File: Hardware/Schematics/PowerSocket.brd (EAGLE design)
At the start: 100 x 47.5 mm, 74 parts, among them T1 BT138-V, T2 BT138-V, T3 BT138-V, T4 BT138-V, T5 BT138-V, T6 BT138-V

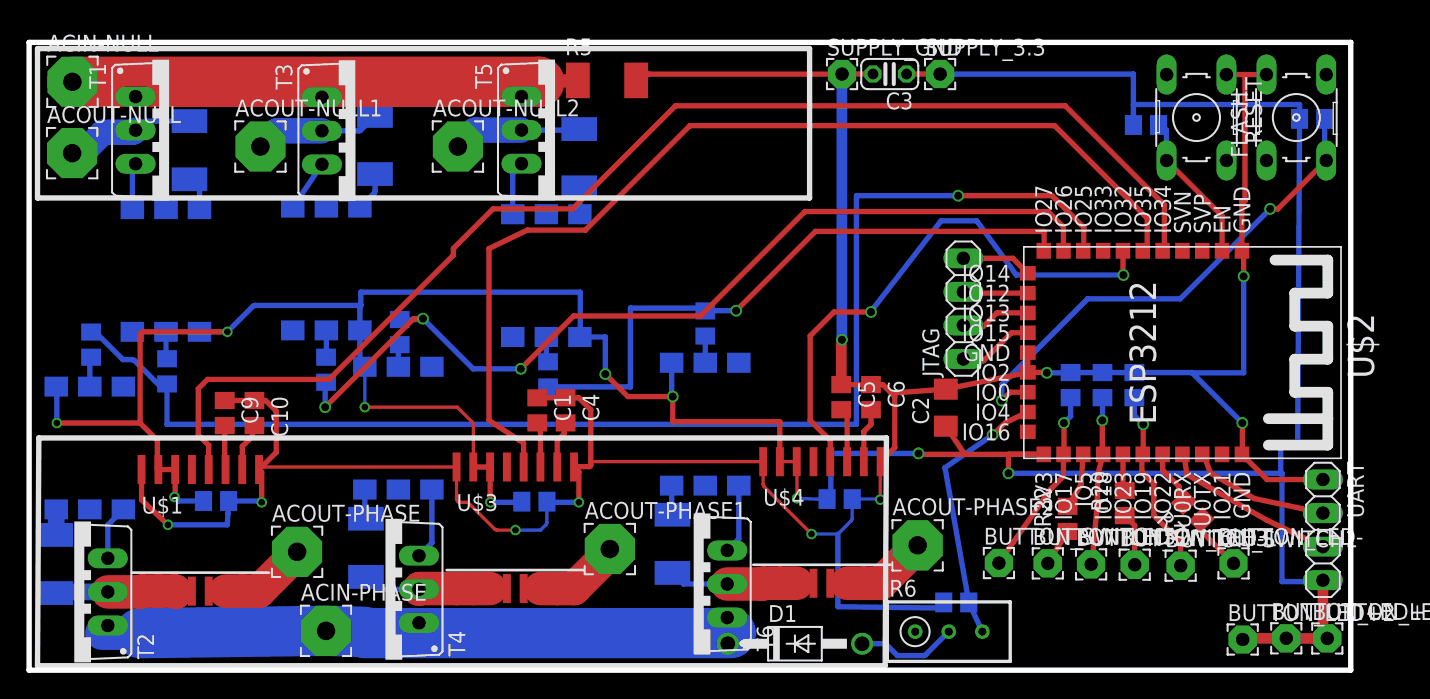
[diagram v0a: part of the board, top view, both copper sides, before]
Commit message: Added more clearance to GND planes.
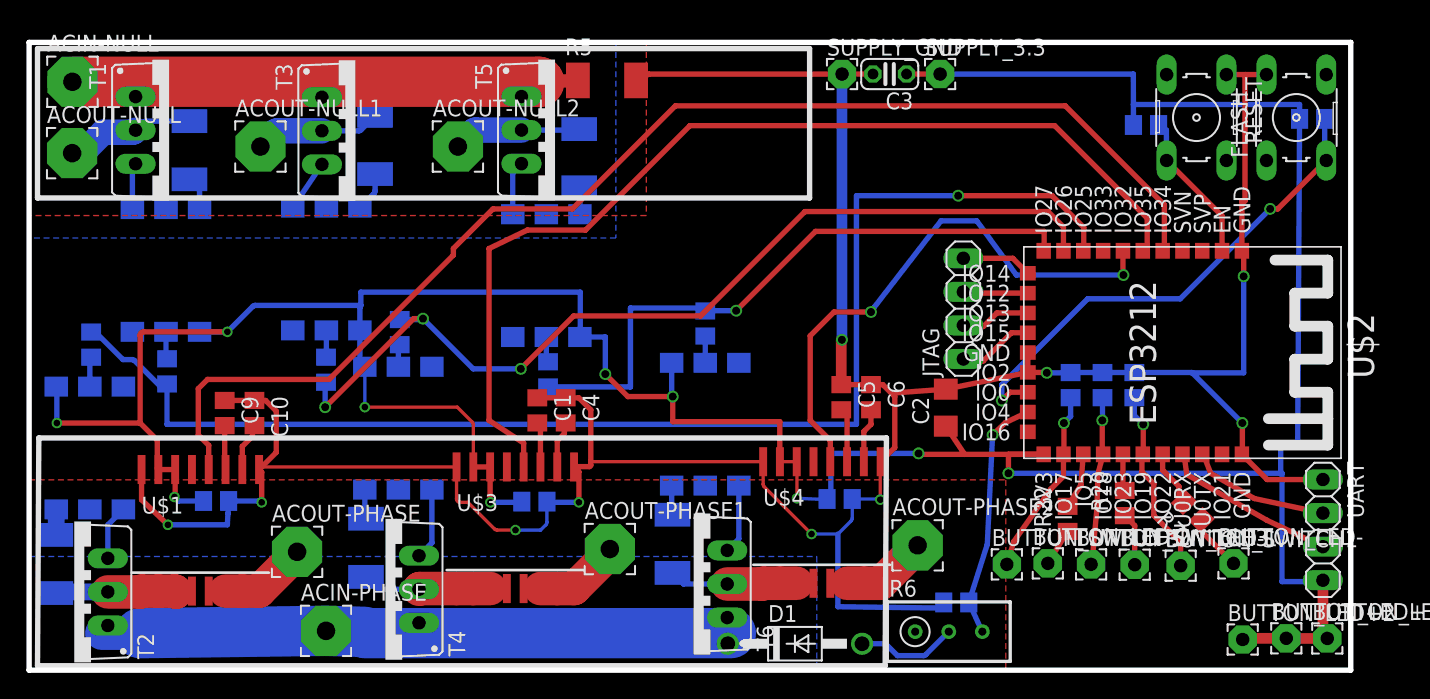
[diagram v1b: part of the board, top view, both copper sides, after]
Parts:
- moved BUTTON_SWITCH5 0.61 mm to (74.0, 9.11)
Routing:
- net N$3: track 20.4 -> 18.6 mm
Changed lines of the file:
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@@
 <element name="BUTTON_LED+2" library="wirepad" package="2,15/1,0" value="-" x="91.825" y="3.42"/>
 <element name="R22" library="rcl" package="R0805" value="100" x="78.58" y="12.545" rot="R90"/>
-<element name="BUTTON_SWITCH5" library="wirepad" package="2,15/1,0" value="-" x="73.38" y="9.205"/>
+<element name="BUTTON_SWITCH5" library="wirepad" package="2,15/1,0" value="-" x="73.98" y="9.105"/>
 <element name="R23" library="rcl" package="R0805" value="10K" x="78.805" y="22.67" rot="MR270"/>
 <element name="JTAG" library="pinhead" package="1X04" value="-" x="70.69" y="28.455" rot="R90"/>
@@
 <wire x1="61.5" y1="26.1" x2="61.5" y2="46.195" width="0.8128" layer="16"/>
 <wire x1="61.5" y1="46.195" x2="61.51" y2="46.205" width="0.8128" layer="16"/>
-<polygon width="0.4064" layer="16" isolate="0.8128">
-<vertex x="0" y="1.2"/>
-<vertex x="0" y="48.6"/>
+<polygon width="0.4064" layer="16" isolate="0.254">
+<vertex x="0" y="9.7"/>
+<vertex x="59.6" y="9.7"/>
+<vertex x="59.6" y="1.1"/>
+<vertex x="100" y="1.1"/>
 <vertex x="100" y="48.6"/>
-<vertex x="100" y="48.5"/>
-<vertex x="100" y="1"/>
-<vertex x="0" y="1"/>
+<vertex x="44.4" y="48.6"/>
+<vertex x="44.4" y="33.8"/>
+<vertex x="0" y="33.8"/>
 </polygon>
 </signal>
@@
 <wire x1="72.125" y1="4.015" x2="72.105" y2="4.035" width="0.4064" layer="16"/>
 <wire x1="72.105" y1="4.035" x2="71.105" y2="6.225" width="0.4064" layer="16"/>
-<wire x1="71.105" y1="6.225" x2="69.3" y2="16.42" width="0.4064" layer="16"/>
-<wire x1="69.3" y1="16.42" x2="72.9" y2="18.9" width="0.4064" layer="16"/>
+<wire x1="71.105" y1="6.225" x2="72.5" y2="10.62" width="0.4064" layer="16"/>
+<wire x1="72.5" y1="10.62" x2="72.9" y2="18.9" width="0.4064" layer="16"/>
 <via x="72.9" y="18.9" extent="1-16" drill="0.6" shape="square"/>
 <wire x1="72.9" y1="18.9" x2="73.87" y2="19.83" width="0.4064" layer="1"/>
@@
 <wire x1="78.3" y1="19.8" x2="78.3" y2="17.465" width="0.4064" layer="1"/>
 <wire x1="78.3" y1="17.465" x2="78.265" y2="17.43" width="0.4064" layer="1"/>
-<wire x1="73.38" y1="9.205" x2="74.5" y2="10.825" width="0.4064" layer="1"/>
+<wire x1="73.98" y1="9.105" x2="74.5" y2="10.825" width="0.4064" layer="1"/>
 <wire x1="74.5" y1="10.825" x2="77.3" y2="14.8" width="0.4064" layer="1"/>
 <wire x1="77.3" y1="14.8" x2="78.265" y2="15.765" width="0.4064" layer="1"/>
@@
 </signal>
 <signal name="N$37">
-<polygon width="0.4064" layer="1" isolate="0.8128">
+<polygon width="0.4064" layer="1">
+<vertex x="0" y="15.5"/>
+<vertex x="73.9" y="15.5"/>
+<vertex x="73.9" y="1.1"/>
 <vertex x="100" y="1.1"/>
-<vertex x="0" y="1.1"/>
-<vertex x="0" y="48.6"/>
 <vertex x="100" y="48.6"/>
+<vertex x="46.7" y="48.6"/>
+<vertex x="46.7" y="35.5"/>
+<vertex x="0" y="35.5"/>
 </polygon>
 </signal>

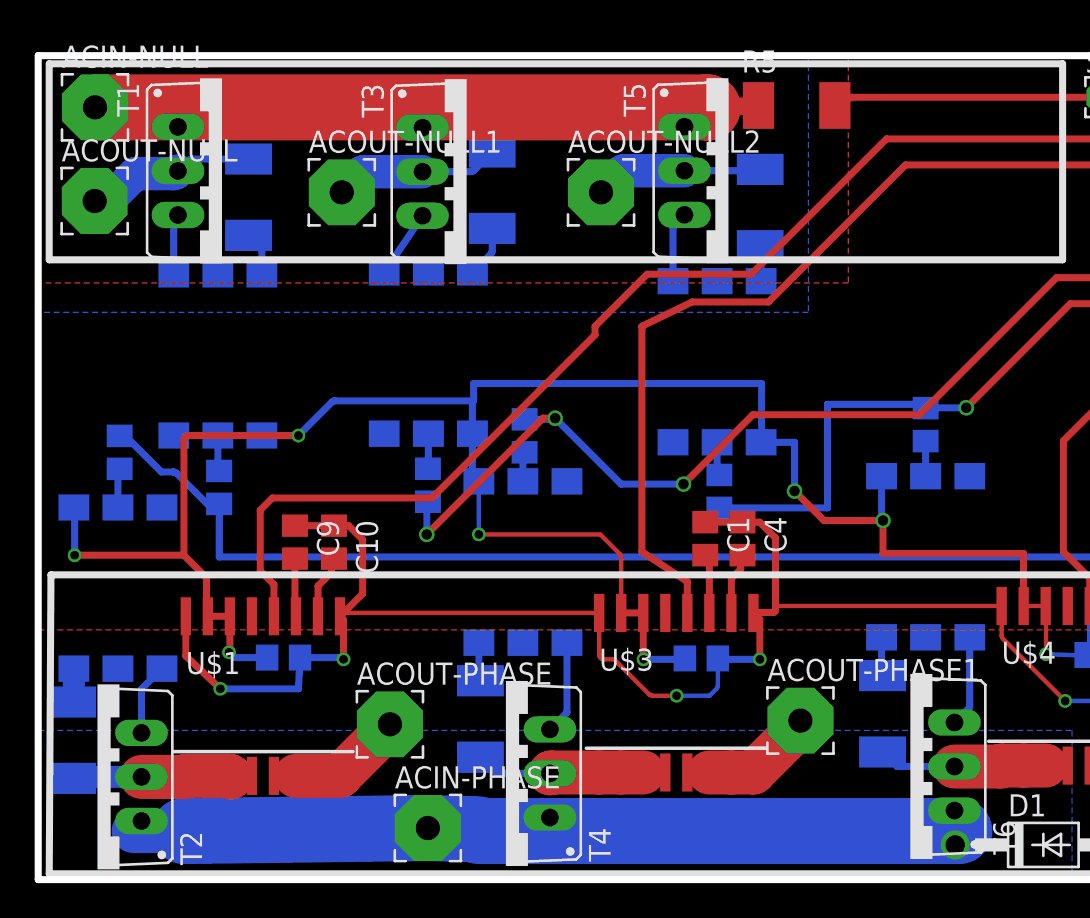
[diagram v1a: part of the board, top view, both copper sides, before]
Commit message: Run AC traces on both sides.
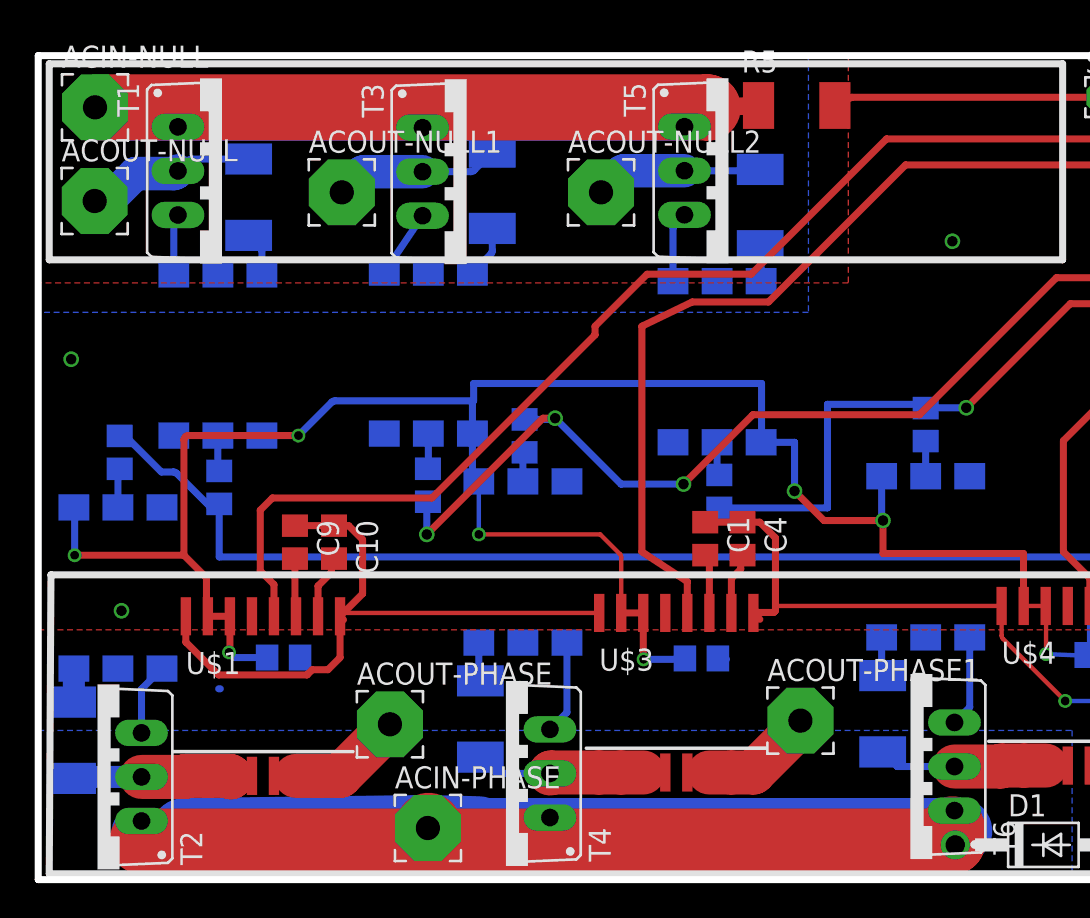
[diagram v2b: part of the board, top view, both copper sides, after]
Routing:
- net N$68: track 0.00 -> 48.6 mm
- net N$37: track 0.00 -> 34.3 mm
- net GND: track 232.6 -> 214.1 mm, vias 10 -> 6
- added copper zone on layer 1, net GND
- removed copper zone on layer 1, net N$37
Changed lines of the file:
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@@
 </class>
 </classes>
-<designrules name="dirt_cheap_dirty_boards.v1">
+<designrules name="dirt_cheap_dirty_boards.v1 *">
 <description language="en">&lt;b&gt;Dirty Cheap Dirty Board Design Rules&lt;/b&gt;
 &lt;br&gt;
@@
 <wire x1="18.7" y1="20.7" x2="18.7" y2="17.58" width="0.4064" layer="1"/>
 <wire x1="18.7" y1="17.58" x2="17.4" y2="16.28" width="0.4064" layer="1"/>
-<wire x1="15.095" y1="13.9" x2="15.045" y2="12.945" width="0.4064" layer="16"/>
-<wire x1="15.045" y1="12.945" x2="15" y2="12.1" width="0.4064" layer="16"/>
-<wire x1="15" y1="12.1" x2="10.5" y2="12.1" width="0.4064" layer="16"/>
 <wire x1="10.4" y1="12.1" x2="10.5" y2="12.1" width="0.4064" layer="16"/>
-<via x="10.5" y="12.1" extent="1-16" drill="0.5" shape="square"/>
-<wire x1="10.5" y1="12.1" x2="8.51" y2="13.99" width="0.4064" layer="1"/>
-<wire x1="8.51" y1="13.99" x2="8.51" y2="16.28" width="0.4064" layer="1"/>
 <wire x1="17.4" y1="16.28" x2="17.5" y2="16.18" width="0.4064" layer="1"/>
 <wire x1="17.4" y1="16.28" x2="17.6" y2="16.08" width="0.4064" layer="1"/>
-<wire x1="17.6" y1="16.08" x2="17.6" y2="13.8" width="0.4064" layer="1"/>
-<via x="17.6" y="13.8" extent="1-16" drill="0.5" shape="square"/>
-<wire x1="17.6" y1="13.8" x2="17.4" y2="13.9" width="0.4064" layer="16"/>
-<wire x1="17.4" y1="13.9" x2="15.095" y2="13.9" width="0.4064" layer="16"/>
 <wire x1="41.23" y1="16.475" x2="41.6" y2="16.105" width="0.4064" layer="1"/>
-<wire x1="41.6" y1="16.105" x2="41.6" y2="13.8" width="0.4064" layer="1"/>
-<via x="41.6" y="13.8" extent="1-16" drill="0.5" shape="square"/>
 <wire x1="39.18" y1="13.85" x2="39.68" y2="13.8" width="0.4064" layer="16"/>
-<wire x1="39.68" y1="13.8" x2="41.6" y2="13.8" width="0.4064" layer="16"/>
 <wire x1="64.43" y1="16.875" x2="64.4" y2="16.802575" width="0.254" layer="1" curve="45"/>
 <wire x1="64.4" y1="16.802575" x2="64.4" y2="14" width="0.254" layer="1"/>
@@
 <wire x1="64.4" y1="14" x2="64.279290625" y2="14.05" width="0.254" layer="16" curve="45"/>
 <wire x1="64.279290625" y1="14.05" x2="62.28" y2="14.05" width="0.254" layer="16"/>
-<wire x1="39.18" y1="13.85" x2="39.18" y2="12.285209375" width="0.254" layer="16"/>
-<wire x1="39.18" y1="12.285209375" x2="39.10560625" y2="12.10560625" width="0.254" layer="16" curve="-44.999502"/>
-<wire x1="39.10560625" y1="12.10560625" x2="38.7" y2="11.7" width="0.254" layer="16"/>
-<wire x1="38.7" y1="11.7" x2="36.8" y2="11.7" width="0.254" layer="16"/>
-<via x="36.8" y="11.7" extent="1-16" drill="0.5" shape="square"/>
-<wire x1="36.8" y1="11.7" x2="35.405209375" y2="11.7" width="0.254" layer="1"/>
-<wire x1="35.405209375" y1="11.7" x2="35.22560625" y2="11.77439375" width="0.254" layer="1" curve="-44.999502"/>
-<wire x1="35.22560625" y1="11.77439375" x2="33.2" y2="13.8" width="0.254" layer="1"/>
-<wire x1="33.2" y1="13.8" x2="32.594" y2="13.8" width="0.254" layer="1"/>
-<wire x1="32.594" y1="13.8" x2="32.34" y2="14.054" width="0.254" layer="1" curve="-90"/>
-<wire x1="32.34" y1="14.054" x2="32.34" y2="16.475" width="0.254" layer="1"/>
 <wire x1="62.28" y1="14.05" x2="62.28" y2="12.585209375" width="0.254" layer="16"/>
 <wire x1="62.28" y1="12.585209375" x2="62.20560625" y2="12.40560625" width="0.254" layer="16" curve="-44.999502"/>
@@
 <vertex x="0" y="33.8"/>
 </polygon>
+<polygon width="0.4064" layer="1">
+<vertex x="0" y="15.5"/>
+<vertex x="73.9" y="15.5"/>
+<vertex x="73.9" y="1.1"/>
+<vertex x="100" y="1.1"/>
+<vertex x="100" y="48.6"/>
+<vertex x="46.7" y="48.6"/>
+<vertex x="46.7" y="35.5"/>
+<vertex x="0" y="35.5"/>
+</polygon>
+<wire x1="8.51" y1="16.28" x2="8.51" y2="14.79" width="0.4064" layer="1"/>
+<wire x1="8.51" y1="14.79" x2="10.4" y2="12.9" width="0.4064" layer="1"/>
+<wire x1="10.4" y1="12.9" x2="15.5" y2="12.9" width="0.4064" layer="1"/>
+<wire x1="15.5" y1="12.9" x2="15.8" y2="13.2" width="0.4064" layer="1"/>
+<wire x1="15.8" y1="13.2" x2="16.7" y2="13.2" width="0.4064" layer="1"/>
+<wire x1="16.7" y1="13.2" x2="17.4" y2="13.9" width="0.4064" layer="1"/>
+<wire x1="17.4" y1="13.9" x2="17.4" y2="16.28" width="0.4064" layer="1"/>
+<wire x1="10.4" y1="12.1" x2="10.4" y2="12.9" width="0" layer="19" extent="1-16"/>
 </signal>
 <signal name="VCC">
@@
 <contactref element="U$4" pad="13"/>
 </signal>
+<signal name="N$61">
+<via x="1.9" y="31.1" extent="1-16" drill="0.6" shape="square"/>
+</signal>
+<signal name="N$66">
+<via x="52.7" y="37.9" extent="1-16" drill="0.6" shape="square"/>
+</signal>
+<signal name="N$67">
+<via x="4.8" y="16.6" extent="1-16" drill="0.6" shape="square"/>
+</signal>
 <signal name="N$37">
-<polygon width="0.4064" layer="1">
-<vertex x="0" y="15.5"/>
-<vertex x="73.9" y="15.5"/>
-<vertex x="73.9" y="1.1"/>
-<vertex x="100" y="1.1"/>
-<vertex x="100" y="48.6"/>
-<vertex x="46.7" y="48.6"/>
-<vertex x="46.7" y="35.5"/>
-<vertex x="0" y="35.5"/>
-</polygon>
+<wire x1="3.3" y1="45.6" x2="37.6" y2="45.6" width="3.81" layer="16"/>
+</signal>
+<signal name="N$68">
+<wire x1="6" y1="4.5" x2="6" y2="3.3" width="1.27" layer="1"/>
+<wire x1="6" y1="3.3" x2="52.7" y2="3.3" width="3.81" layer="1"/>
+<wire x1="52.7" y1="3.3" x2="52.7" y2="4" width="3.81" layer="1"/>
+</signal>
+<signal name="N$69">
+<wire x1="22.5" y1="4" x2="22.5" y2="4.2" width="3.81" layer="1"/>
 </signal>
 </signals>

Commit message: Further routing improvements.
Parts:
- moved R13 2.36 mm to (27.6, 38.9)
- moved R3 2.12 mm to (10.7, 21.6)
- moved R4 1.33 mm to (12.4, 39.1)
- moved OK1 1.20 mm to (10.4, 30.1)
- moved R11 0.80 mm to (71.0, 6.22)
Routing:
- net GND: track 214.1 -> 185.0 mm, vias 6 -> 5
- net N$19: track 3.51 -> 4.71 mm
- net N$14: track 9.60 -> 10.7 mm
- net N$8: track 100.3 -> 101.3 mm
- net N$18: track 2.55 -> 3.50 mm
- net N$6: track 2.06 -> 2.98 mm

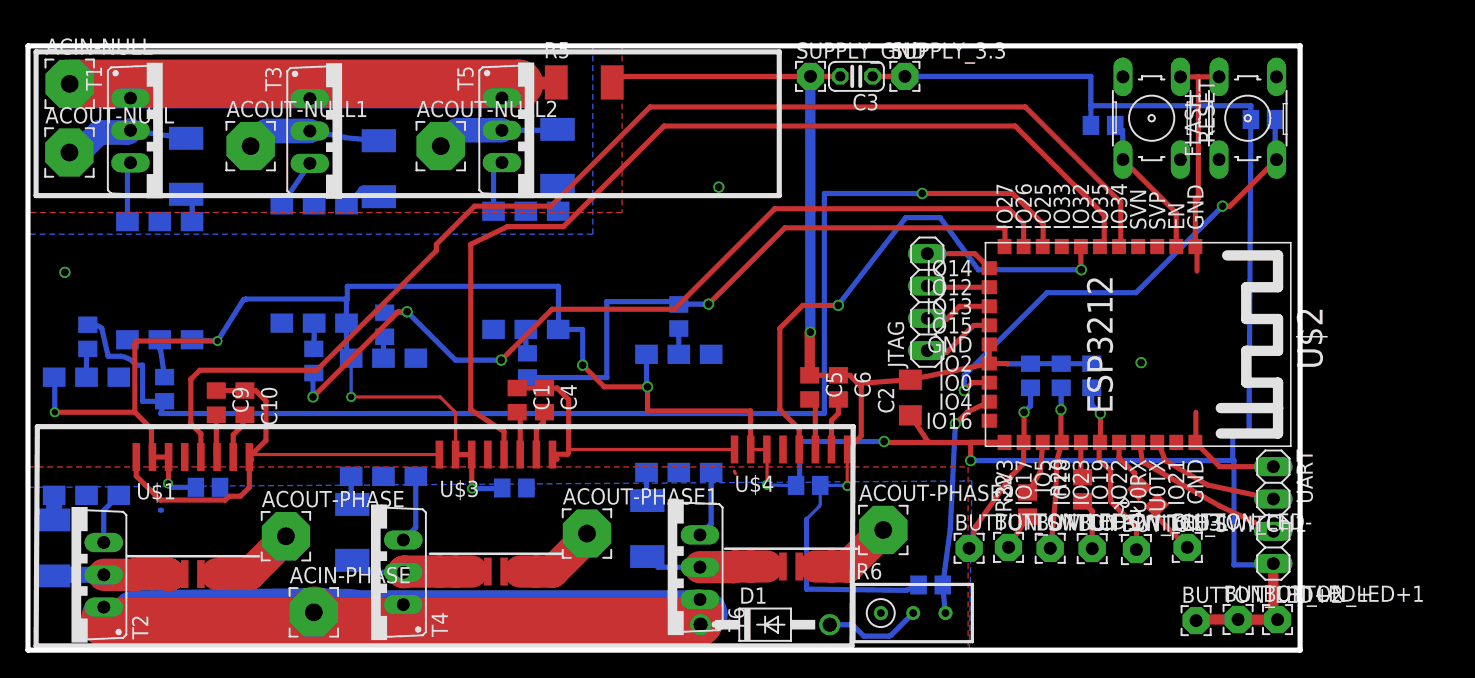
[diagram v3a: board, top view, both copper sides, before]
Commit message: Added mounting holes.
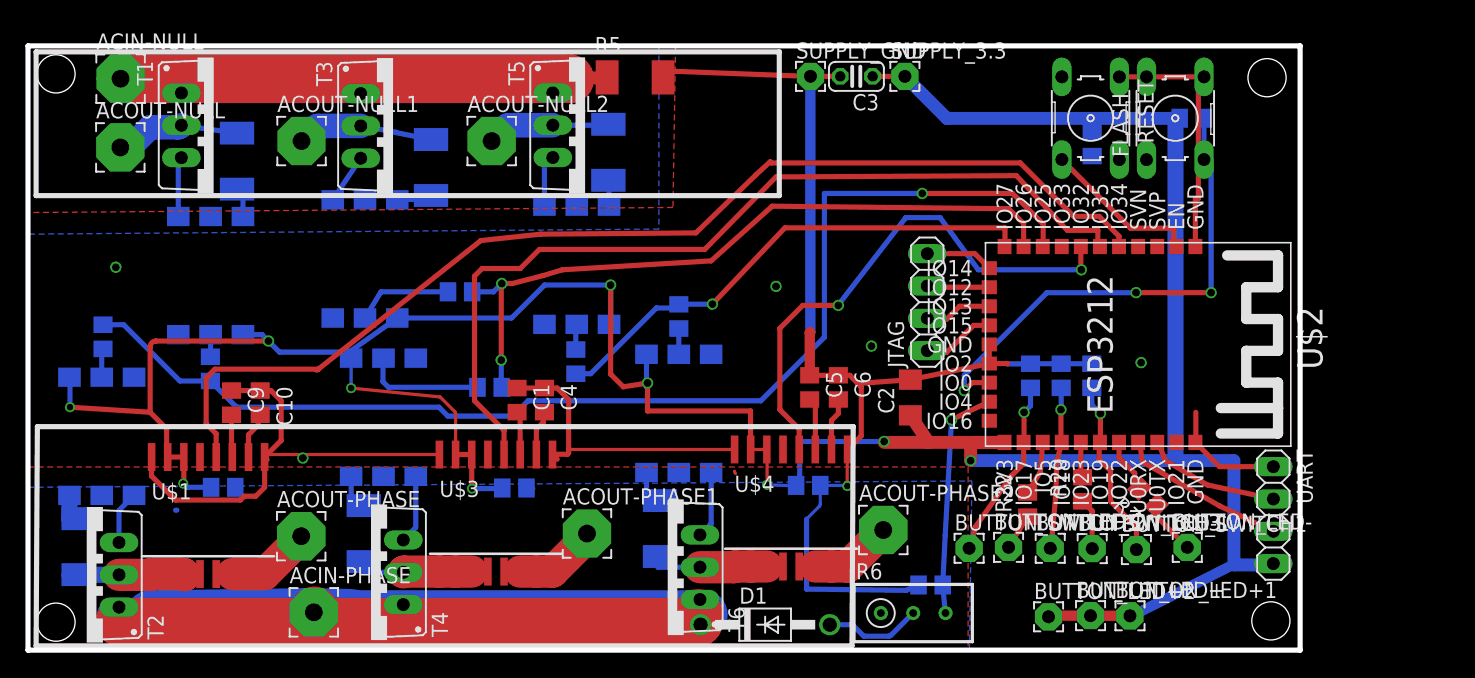
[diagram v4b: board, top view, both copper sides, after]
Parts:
- moved R12 12.7 mm to (34.0, 29.3), turned to 0 degrees
- moved BUTTON_LED+2 11.6 mm to (80.2, 3.72)
- moved BUTTON_LED+ 11.6 mm to (83.5, 3.81)
- moved BUTTON_LED+1 11.6 mm to (86.6, 3.80)
- moved R14 9.60 mm to (36.3, 21.8), turned to 180 degrees
- moved FLASH 5.70 mm to (90.2, 42.9)
- moved R2 5.60 mm to (91.5, 42.9)
- moved RESET 4.80 mm to (83.5, 42.9)
- moved R13 4.10 mm to (31.7, 39.0)
- moved ACIN-NULL 4.02 mm to (7.28, 46.0)
- moved T3 4.02 mm to (28.7, 42.3)
- moved ACOUT-NULL 4.02 mm to (7.25, 40.6)
- moved ACOUT-NULL1 4.02 mm to (21.5, 41.1)
- moved ACOUT-NULL2 4.02 mm to (36.4, 41.1)
- moved OK1 4.02 mm to (14.4, 30.5)
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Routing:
- net N$25: track 71.1 -> 55.9 mm, vias 3 -> 2
- net N$8: track 101.3 -> 93.5 mm
- net N$32: track 1.72 -> 9.48 mm
- net N$54: track 47.7 -> 40.1 mm
- net N$12: track 95.3 -> 87.8 mm
- net N$11: track 76.8 -> 70.5 mm
- net VCC: track 258.7 -> 252.8 mm
- net N$28: track 2.03 -> 7.68 mm
- net GND: track 185.0 -> 181.0 mm, vias 5 -> 6
- net N$7: track 38.3 -> 39.8 mm, vias 2 -> 3
- net N$6: track 2.98 -> 1.75 mm
- net N$68: track 48.6 -> 47.4 mm
- net N$51: track 60.0 -> 58.8 mm
- net N$47: track 2.23 -> 3.21 mm
- net N$2: track 11.6 -> 12.6 mm
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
